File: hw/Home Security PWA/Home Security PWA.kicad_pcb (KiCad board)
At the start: 2 copper layers, 77.5 x 111.8 mm, 52 parts, among them J1 Conn_01x10_Pin, J10 1825960000, J11 1825960000, J12 1825960000, J13 1825960000, J14 1825960000, J15 1825960000, J16 1825960000, J17 1825960000, J18 1825960000, J19 1825960000, J2 Conn_01x10_Pin, J20 1825960000, J21 1825960000, J22 1825960000, J23 1825960000, J24 1825960000, J25 1825960000, J26 1825960000, J27 1825960000, J28 1825960000, J29 1825960000, J3 1825960000, J30 1825960000, J31 1825960000, J32 1825960000, J33 1825960000, J34 1825960000, J4 1825960000, J5 1825960000, J6 1825960000, J7 1825960000, J8 1825960000, J9 1825960000, U1 ADS1115IDGS, U2 ADS1115IDGS, U3 MCP23017_SO

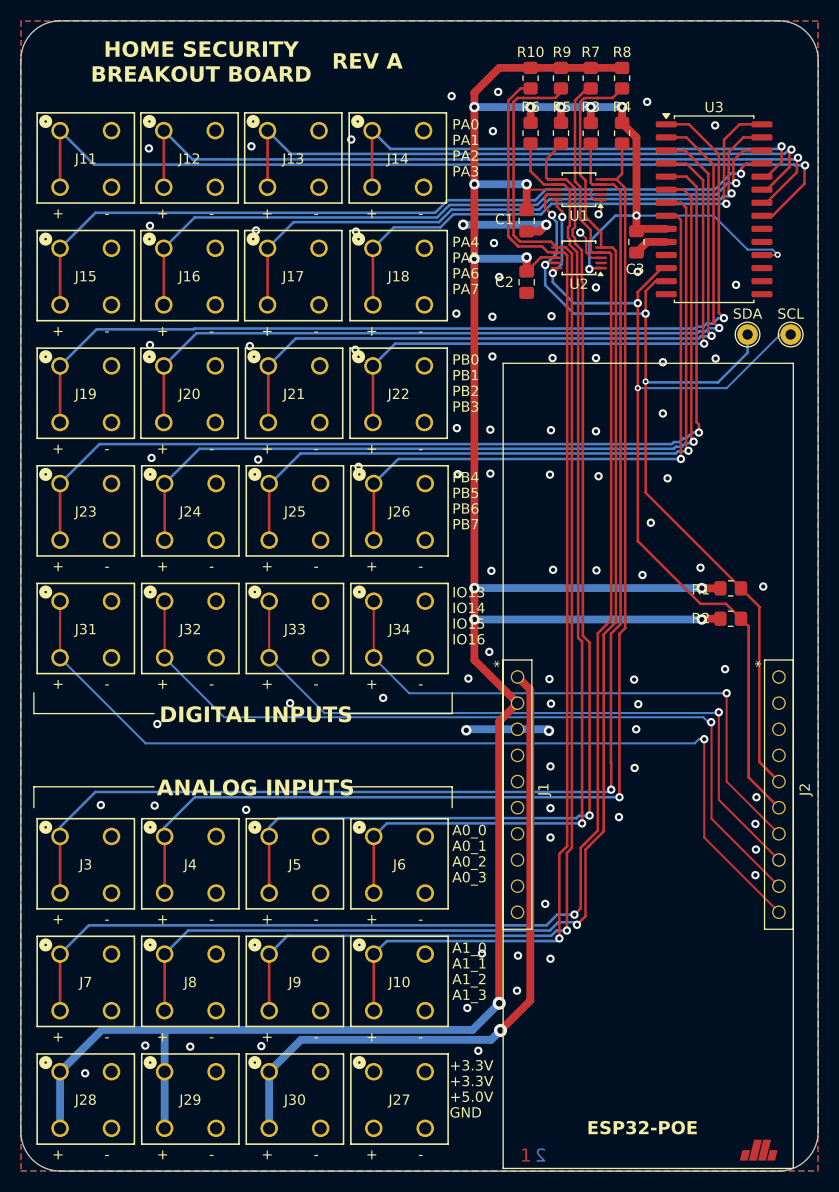
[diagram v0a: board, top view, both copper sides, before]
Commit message: Remove these "per project" components.
Updates to Home Security with Inventree, new symbols, new schematics.
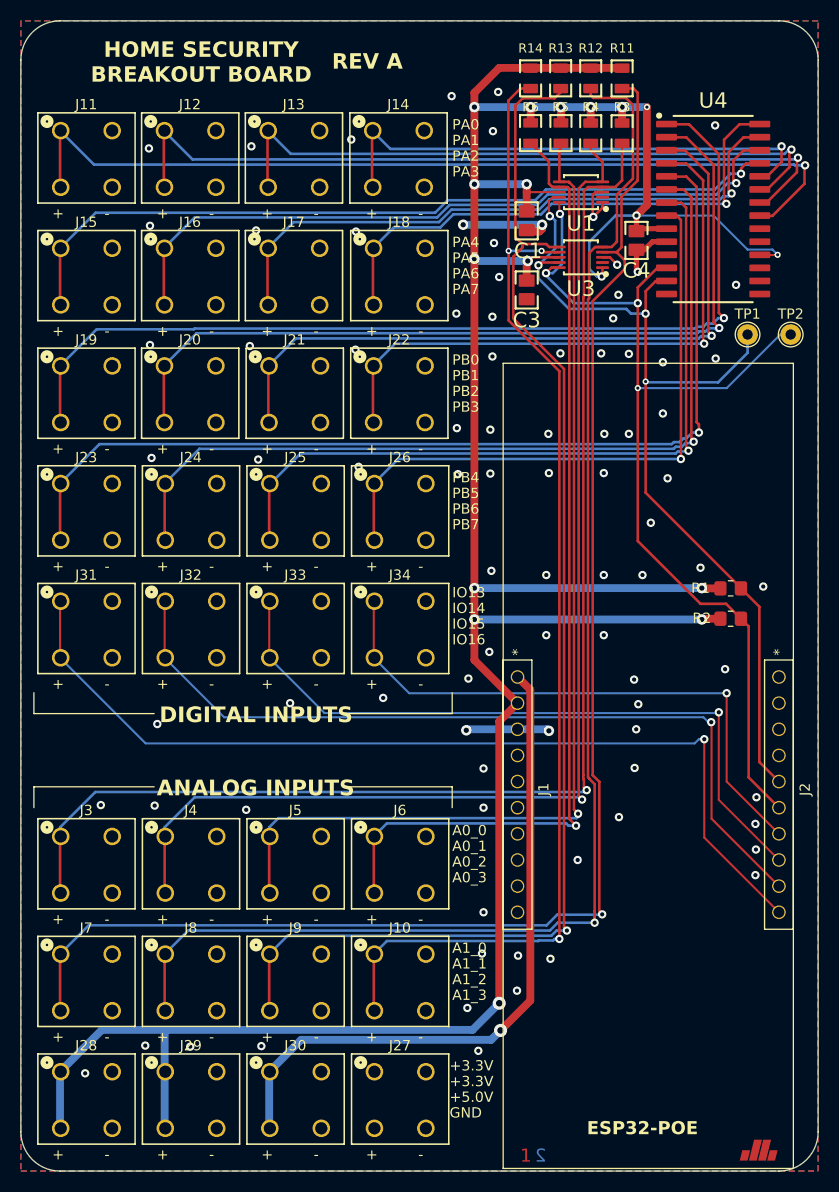
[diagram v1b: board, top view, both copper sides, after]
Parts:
- removed C2: .1uF, Capacitor_SMD:C_0805_2012Metric_Pad1.18x1.45mm_HandSolder
- removed R10, R7, R8, R9: 10K, Resistor_SMD:R_0805_2012Metric_Pad1.20x1.40mm_HandSolder
- removed SCL, SDA: TestPoint, TestPoint:TestPoint_THTPad_D2.0mm_Drill1.0mm
- removed U2: ADS1115IDGS, Package_SO:TSSOP-10_3x3mm_P0.5mm
- added C4: J00005, JLibrary:CAPC201X125X100L50M, F.Cu at (151.3, 68.3)
- added R11: J00001, JLibrary:RESC2012X60M, F.Cu at (149.9, 52.6)
- added R12: J00001, JLibrary:RESC2012X60M, F.Cu at (146.8, 52.6)
- added R13: J00001, JLibrary:RESC2012X60M, F.Cu at (143.9, 52.6)
- added R14: J00001, JLibrary:RESC2012X60M, F.Cu at (141.0, 52.6)
- added TP1: TestPoint, TestPoint:TestPoint_THTPad_D2.0mm_Drill1.0mm, F.Cu at (162.1, 77.5)
- added TP2: TestPoint, TestPoint:TestPoint_THTPad_D2.0mm_Drill1.0mm, F.Cu at (166.2, 77.5)
- added U4: J00004, JLibrary:SOIC127P1030X265-28M, F.Cu at (158.7, 65.3)
- C1, C3: value .1uF -> J00005; footprint Capacitor_SMD:C_0805_2012Metric_Pad1.18x1.45mm_HandSolder -> JLibrary:CAPC201X125X100L50M
- J10, J11, J12, J13, J14, J15, J16, J17, J18, J19, J20, J21, J22, J23, J24, J25, J26, J27, J28, J29, J3, J30, J31, J32, J33, J34, J4, J5, J6, J7, J8, J9: value 1825960000 -> J00006; footprint footprint:CONN_1825960000_WED -> JLibrary:J00006
- R3, R4, R5, R6: value 10K -> J00001; footprint Resistor_SMD:R_0805_2012Metric_Pad1.20x1.40mm_HandSolder -> JLibrary:RESC2012X60M
- U1: value ADS1115IDGS -> J00003; footprint Package_SO:TSSOP-10_3x3mm_P0.5mm -> JLibrary:SOP10P50_300X490X110L55X22M
- U3: value MCP23017_SO -> J00003; footprint Package_SO:SOIC-28W_7.5x17.9mm_P1.27mm -> JLibrary:SOP10P50_300X490X110L55X22M
- moved U3 13.8 mm to (145.9, 70.0), turned to 180 degrees
- moved C3 11.6 mm to (140.6, 73.1)
- moved J14 3.59 mm to (128.1, 60.2)
- moved J15 3.59 mm to (97.8, 71.6)
- moved J16 3.59 mm to (107.9, 71.6)
- moved J17 3.59 mm to (118.0, 71.6)
- moved J19 3.59 mm to (97.8, 83.1)
- moved J20 3.59 mm to (107.9, 83.1)
- moved J21 3.59 mm to (118.0, 83.1)
- moved J23 3.59 mm to (97.8, 94.5)
- moved J24 3.59 mm to (108.0, 94.5)
- moved J25 3.59 mm to (118.1, 94.5)
- moved J26 3.59 mm to (128.3, 94.5)
- moved J31 3.59 mm to (97.8, 105.9)
- moved J32 3.59 mm to (108.0, 105.9)
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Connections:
- R3 pad 1: +3.3V -> /ADC0_0
- R3 pad 2: /ADC0_0 -> +3.3V
- R4 pad 1: +3.3V -> /ADC0_1
- R4 pad 2: /ADC0_1 -> +3.3V
- R5 pad 1: +3.3V -> /ADC0_2
- R5 pad 2: /ADC0_2 -> +3.3V
- R6 pad 1: +3.3V -> /ADC0_3
- R6 pad 2: /ADC0_3 -> +3.3V
- U3 pad 1: /PB0 -> +3.3V
- U3 pad 10: GND -> /SCL
- U3 pad 2: /PB1 -> unconnected-(U3-ALERT/RDY-Pad2)
- U3 pad 3: /PB2 -> GND
- U3 pad 4: /PB3 -> /ADC1_0
- U3 pad 5: /PB4 -> /ADC1_1
- U3 pad 6: /PB5 -> /ADC1_2
- U3 pad 7: /PB6 -> /ADC1_3
- U3 pad 8: /PB7 -> +3.3V
- U3 pad 9: +3.3V -> /SDA
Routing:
- net +3.3V: track 296.6 -> 302.8 mm, vias 17 -> 18
- net /ADC1_0: track 142.1 -> 145.5 mm
- net /ADC0_2: track 107.0 -> 103.7 mm
- net /ADC0_1: track 117.6 -> 114.6 mm
- net /ADC1_3: track 113.3 -> 115.3 mm, vias 1 -> 3
- net /ADC0_0: track 127.1 -> 125.2 mm
- net /SCL: track 97.5 -> 98.8 mm
- net /ADC1_2: track 126.1 -> 127.3 mm
- net /ADC1_1: track 135.2 -> 136.2 mm
- net /ADC0_3: track 95.7 -> 94.8 mm
- net /SDA: track 91.6 -> 92.4 mm
- net GND: track 29.7 -> 30.0 mm, vias 87 -> 88

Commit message: More work.
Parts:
- removed the J1 at (139.7, 110.7)
- removed the J2 at (165.1, 110.7)
- added J21: J00007, JLibrary:RHDRV10W64P254_10X1_2590X254H850, F.Cu at (230.5, 161.7)
- added J22: J00007, JLibrary:RHDRV10W64P254_10X1_2590X254H850, F.Cu at (255.9, 161.7)
- added U4: J00008, JLibrary:J00008, F.Cu at (243.2, 157.2)
- moved TP1 99.6 mm to (254.0, 115.7)
- moved J13 99.0 mm to (188.6, 134.0)
- moved J14 99.0 mm to (198.8, 134.0)
- moved J15 99.0 mm to (208.9, 134.0)
- moved J23 99.0 mm to (188.6, 168.3)
- moved J24 99.0 mm to (198.8, 168.3)
- moved J25 99.0 mm to (208.9, 168.3)
- moved J27 99.0 mm to (188.6, 179.7)
- moved J28 99.0 mm to (198.8, 179.7)
- moved J29 99.0 mm to (208.9, 179.7)
- moved C1 99.0 mm to (231.4, 105.9)
- moved C2 99.0 mm to (242.1, 107.8)
- moved C3 99.0 mm to (231.4, 112.6)
- moved J10 99.0 mm to (198.7, 122.6)
- moved J11 99.0 mm to (208.8, 122.6)
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- renumbered C4 to C2, J11 to J1, J20 to J10, J21 to J11, J22 to J12, J23 to J13, J24 to J14, J25 to J15, J26 to J16, J31 to J17, J32 to J18, J33 to J19, J12 to J2, J34 to J20, J3 to J23, J4 to J24, J5 to J25, J6 to J26, J7 to J27, J8 to J28, J9 to J29, J13 to J3, J10 to J30, J28 to J31, J29 to J32, J30 to J33, J27 to J34, J14 to J4, J15 to J5, J16 to J6, J17 to J7, J18 to J8, J19 to J9, R14 to R1, R2 to R10, R13 to R2, R12 to R3, R11 to R4, R6 to R5, R5 to R6, R4 to R7, R3 to R8, R1 to R9, U4 to U2
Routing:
- net +3.3V: track 302.8 -> 294.2 mm
- net /GPIO13: track 91.5 -> 94.6 mm
- net /GPIO14: track 79.9 -> 82.9 mm
- net /GPIO15: track 68.2 -> 71.2 mm
- net /SDA: track 92.4 -> 94.7 mm
- net /GPIO16: track 57.0 -> 58.9 mm
- net /ADC0_3: track 94.8 -> 96.4 mm
- net /ADC0_0: track 125.2 -> 123.8 mm
- net /ADC0_1: track 114.6 -> 114.0 mm
- net GND: vias 88 -> 89
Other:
- board size 77.5 x 111.8 mm -> 83.8 x 111.8 mm
- board text added: "SCL"
- board text added: "SDA"

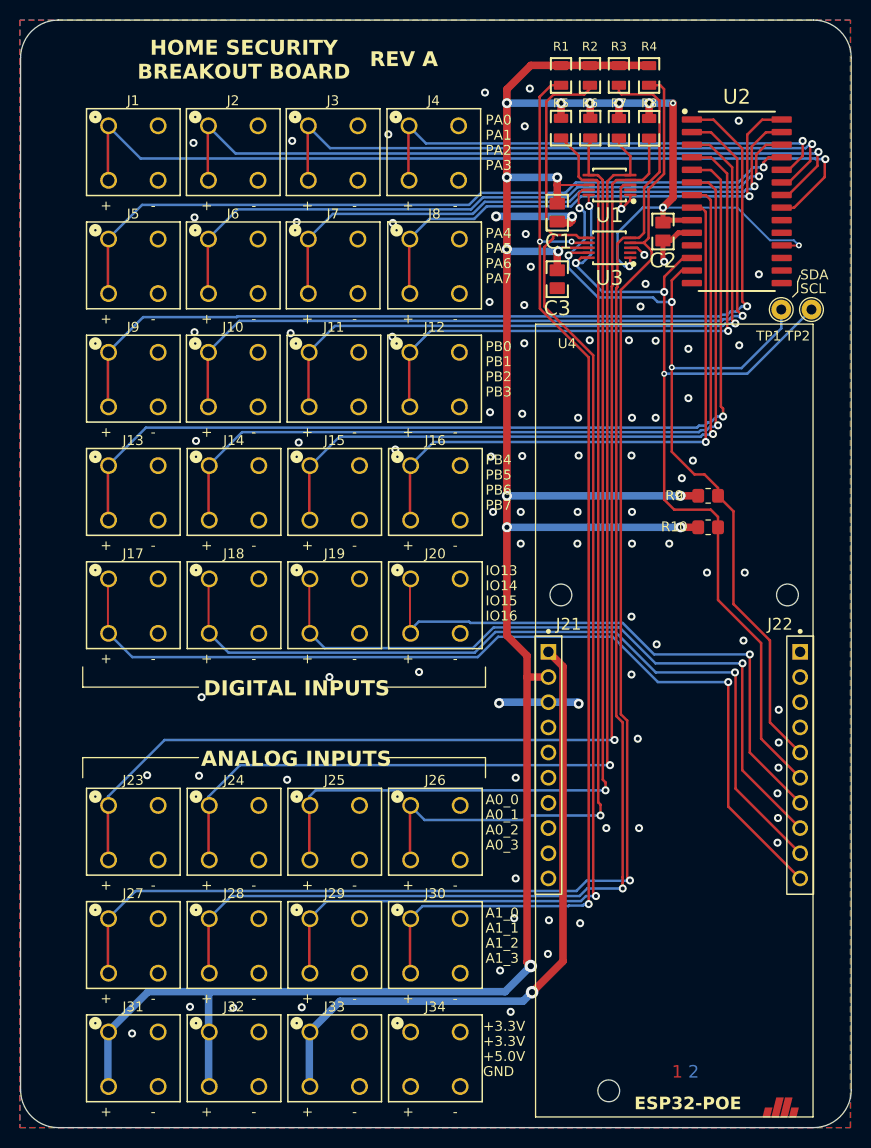
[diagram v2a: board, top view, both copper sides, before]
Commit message: Using all custom symbols/footprints.
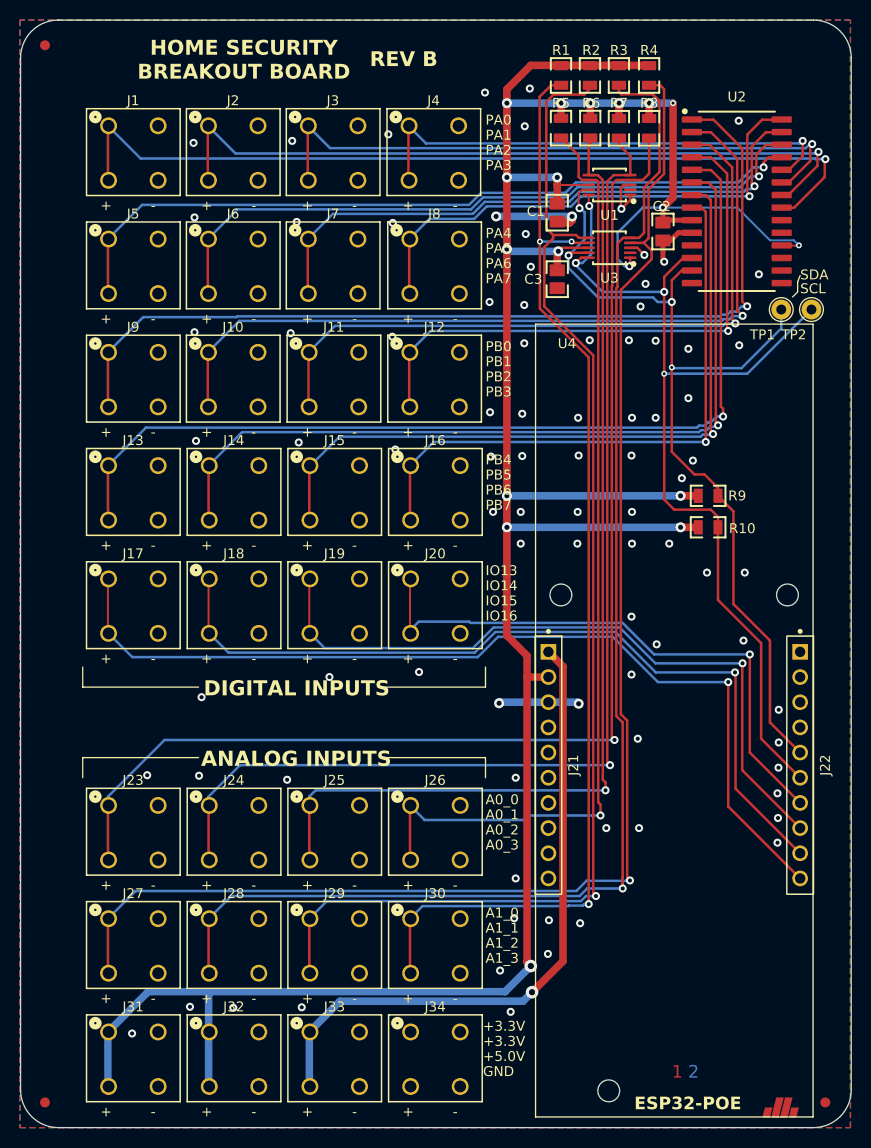
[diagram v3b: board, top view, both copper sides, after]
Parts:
- added FID1: ~, JLibrary:FIDUCIAL_1MM, F.Cu at (179.7, 89.0)
- added FID2: ~, JLibrary:FIDUCIAL_1MM, F.Cu at (179.7, 195.7)
- added FID3: ~, JLibrary:FIDUCIAL_1MM, F.Cu at (258.4, 195.7)
- R1, R2, R3, R4, R5, R6, R7, R8: value J00001 -> J00009
- R10, R9: value 4.7K -> J00001; footprint Resistor_SMD:R_0805_2012Metric_Pad1.20x1.40mm_HandSolder -> JLibrary:RESC2012X60M
- TP1, TP2: value TestPoint -> ~; footprint TestPoint:TestPoint_THTPad_D2.0mm_Drill1.0mm -> JLibrary:TESTPOINT_TH_1MMD
- turned R10 to 180 degrees
- turned R9 to 180 degrees
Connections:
- R10 pad 1: +3.3V -> /SCL
- R10 pad 2: /SCL -> +3.3V
- R9 pad 1: +3.3V -> /SDA
- R9 pad 2: /SDA -> +3.3V
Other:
- board text added: "REV B"
- board text removed: "REV A"

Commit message: Updates.
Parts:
- added REF**: INFO, JLibrary:INFO, F.Cu at (196.2, 160.1)
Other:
- board text added: "PWR"
- board text removed: "REV B"
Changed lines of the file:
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@@
 		)
 	)
+	(footprint "JLibrary:INFO"
+		(layer "F.Cu")
+		(at 196.215 160.147)
+		(property "Reference" "REF**"
+			(at 0 -0.5 0)
+			(unlocked yes)
+			(layer "F.SilkS")
+			(hide yes)
+			(effects
+				(font
+					(size 1 1)
+					(thickness 0.15)
+				)
+			)
+		)
+		(property "Value" "INFO"
+			(at 0 1 0)
+			(unlocked yes)
+			(layer "F.Fab")
+			(hide yes)
+			(effects
+				(font
+					(size 1 1)
+					(thickness 0.15)
+				)
+			)
+		)
+		(property "Datasheet" ""
+			(at 0 0 0)
+			(unlocked yes)
+			(layer "F.Fab")
+			(hide yes)
+			(effects
+				(font
+					(size 1 1)
+					(thickness 0.15)
+				)
+			)
+		)
+		(property "Description" ""
+			(at 0 0 0)
+			(unlocked yes)
+			(layer "F.Fab")
+			(hide yes)
+			(effects
+				(font
+					(size 1 1)
+					(thickness 0.15)
+				)
+			)
+		)
+		(attr smd exclude_from_pos_files exclude_from_bom)
+		(fp_rect
+			(start 0 -2.54)
+			(end 15.24 0)
+			(stroke
+				(width 0.12)
+				(type solid)
+			)
+			(fill yes)
+			(layer "F.SilkS")
+		)
+		(fp_text user "JA00001"
+			(at 0 -5.715 0)
+			(unlocked yes)
+			(layer "F.SilkS")
+			(effects
+				(font
+					(size 1 1)
+					(thickness 0.2)
+					(bold yes)
+				)
+				(justify left)
+			)
+		)
+		(fp_text user "REV B"
+			(at 0 -3.175 0)
+			(unlocked yes)
+			(layer "F.SilkS")
+			(effects
+				(font
+					(size 1 1)
+					(thickness 0.15)
+				)
+				(justify left bottom)
+			)
+		)
+		(embedded_fonts no)
+	)
 	(footprint "JLibrary:RESC2012X60M"
 		(layer "F.Cu")
@@
 	)
 	(gr_line
-		(start 195.199 160.909)
-		(end 183.515 160.909)
+		(start 181.61 195.707)
+		(end 181.61 194.437)
 		(stroke
 			(width 0.1)
@@
 	)
 	(gr_line
-		(start 213.741 160.909)
-		(end 224.155 160.909)
+		(start 181.61 164.592)
+		(end 181.61 163.957)
 		(stroke
 			(width 0.1)
@@
 	)
 	(gr_line
-		(start 224.155 160.909)
-		(end 224.155 162.941)
+		(start 181.61 95.377)
+		(end 182.88 95.377)
 		(stroke
 			(width 0.1)
@@
 	)
 	(gr_line
-		(start 183.515 160.909)
-		(end 183.515 162.941)
+		(start 181.61 188.087)
+		(end 181.61 186.817)
+		(stroke
+			(width 0.1)
+			(type default)
+		)
+		(layer "F.SilkS")
+	)
+	(gr_line
+		(start 181.61 186.817)
+		(end 182.88 186.817)
+		(stroke
+			(width 0.1)
+			(type default)
+		)
+		(layer "F.SilkS")
+	)
+	(gr_line
+		(start 181.61 112.522)
+		(end 181.61 95.377)
 		(stroke
 			(width 0.1)
@@
 	)
 	(gr_line
+		(start 181.61 183.642)
+		(end 181.61 184.277)
+		(stroke
+			(width 0.1)
+			(type default)
+		)
+		(layer "F.SilkS")
+	)
+	(gr_line
+		(start 181.61 132.842)
+		(end 181.61 149.987)
+		(stroke
+			(width 0.1)
+			(type default)
+		)
+		(layer "F.SilkS")
+	)
+	(gr_line
 		(start 255.905 112.268)
 		(end 255.651 112.903)
@@
 	)
 	(gr_line
-		(start 195.199 153.797)
-		(end 183.515 153.797)
+		(start 181.61 184.277)
+		(end 182.88 184.277)
 		(stroke
 			(width 0.1)
@@
 	)
 	(gr_line
-		(start 224.155 153.797)
-		(end 224.155 151.765)
+		(start 181.61 149.987)
+		(end 182.88 149.987)
 		(stroke
 			(width 0.1)
@@
 	)
 	(gr_line
-		(start 255.651 112.903)
-		(end 255.651 113.919)
+		(start 181.61 163.957)
+		(end 182.88 163.957)
 		(stroke
 			(width 0.1)
@@
 	)
 	(gr_line
-		(start 213.741 153.797)
-		(end 224.155 153.797)
+		(start 181.61 195.707)
+		(end 182.88 195.707)
 		(stroke
 			(width 0.1)
@@
 	)
 	(gr_line
-		(start 183.515 153.797)
-		(end 183.515 151.765)
+		(start 255.651 112.903)
+		(end 255.651 113.919)
 		(stroke
 			(width 0.1)
@@
 	)
 	(gr_text "HOME SECURITY\nBREAKOUT BOARD"
-		(at 199.771 92.583 0)
+		(at 203.835 92.583 0)
 		(layer "F.SilkS")
 		(effects
@@
 		)
 	)
-	(gr_text "REV B"
-		(at 212.471 91.313 0)
-		(layer "F.SilkS")
-		(effects
-			(font
-				(size 1.5 1.5)
-				(thickness 0.3)
-				(bold yes)
-			)
-			(justify left bottom)
-		)
-	)
 	(gr_text "IO15"
 		(at 224.155 145.669 0)
@@
 	)
 	(gr_text "ANALOG INPUTS"
-		(at 195.453 161.925 0)
+		(at 182.245 183.007 90)
 		(layer "F.SilkS")
 		(effects
@@
 		)
 	)
+	(gr_text "PWR"
+		(at 182.245 193.802 90)
+		(layer "F.SilkS")
+		(effects
+			(font
+				(size 1.524 1.524)
+				(thickness 0.381)
+				(bold yes)
+			)
+			(justify left bottom)
+		)
+	)
 	(gr_text "SCL"
 		(at 255.905 114.173 0)
@@
 	)
 	(gr_text "DIGITAL INPUTS"
-		(at 195.707 154.813 0)
+		(at 182.245 131.572 90)
 		(layer "F.SilkS")
 		(effects
